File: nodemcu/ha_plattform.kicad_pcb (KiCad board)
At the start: 2 copper layers, 54 x 55 mm, 4 parts

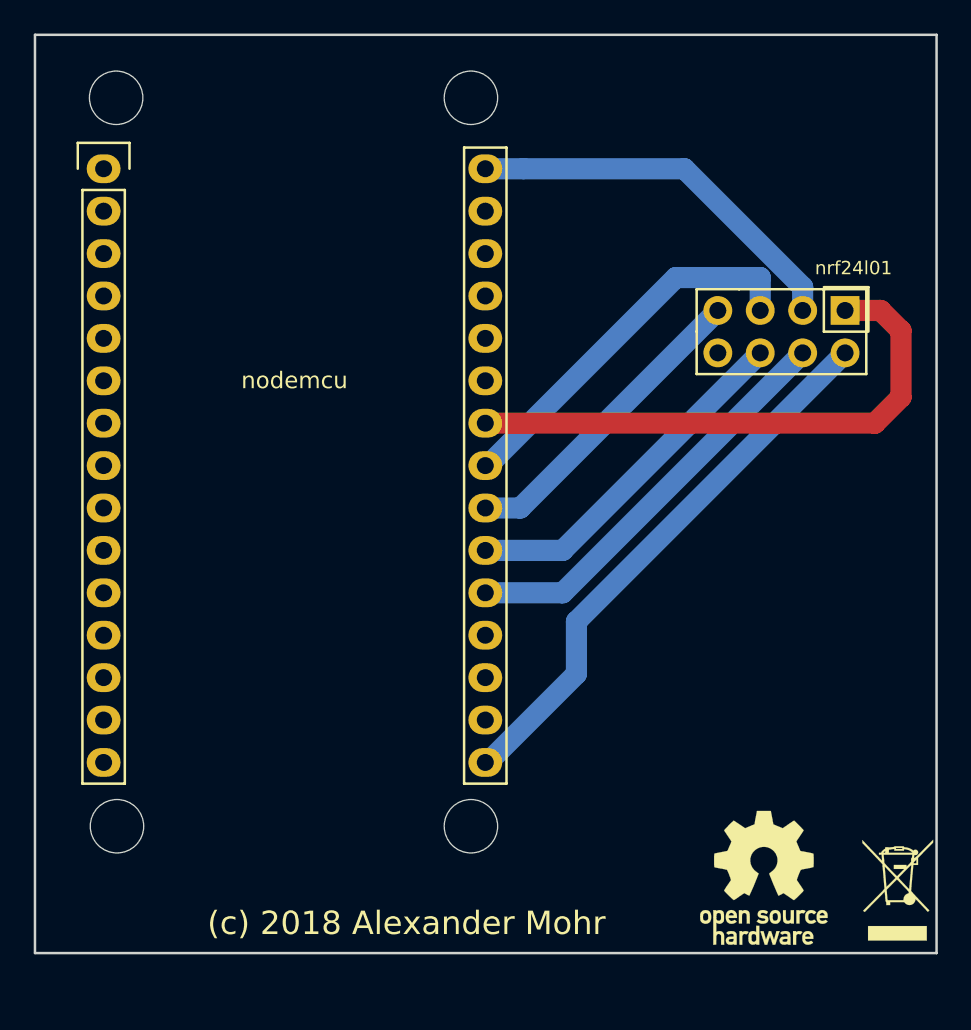
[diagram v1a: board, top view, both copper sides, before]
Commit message: fixed size for node mcu
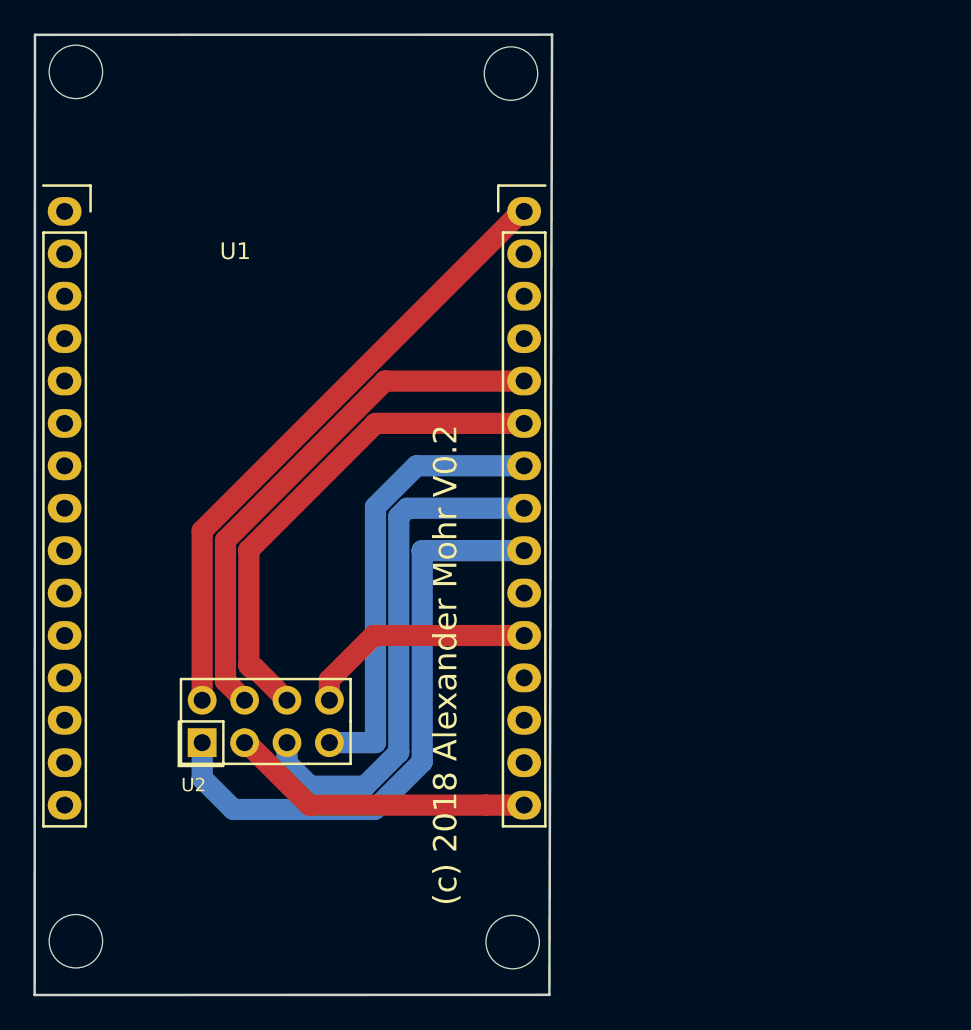
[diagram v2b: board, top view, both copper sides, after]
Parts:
- removed REF**: OSHW-Logo_7.5x8mm_SilkScreen, Symbol:OSHW-Logo_7.5x8mm_SilkScreen
- removed REF**: WEEE-Logo_4.2x6mm_SilkScreen, Symbol:WEEE-Logo_4.2x6mm_SilkScreen
- removed nodemcu: NodeMCU_Amica_R2, nodemcu:NodeMCU_Amica_R2
- removed nrf24l01: nRF24L01+, mysensors_radios:NRF24L01
- added U1: NodeMCU_Amica_R2, nodemcu:NodeMCU_personal, F.Cu at (20.6, 20.3)
- added U2: nRF24L01+, mysensors_radios:NRF24L01, F.Cu at (28.5, 63.9)
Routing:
- net (no net): track 0.00 -> 14.0 mm
- net Net-(U1-Pad21): track 21.4 -> 29.7 mm
- net Net-(U1-Pad23): track 23.1 -> 31.2 mm
- net Net-(U1-Pad22): track 18.8 -> 26.8 mm
- net Net-(U1-Pad20): track 25.0 -> 31.9 mm
- net Net-(U1-Pad30): track 23.3 -> 18.3 mm
- net Net-(U1-Pad16): track 33.5 -> 37.4 mm
- net Net-(U1-Pad24): track 33.4 -> 36.0 mm
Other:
- board size 54 x 55 mm -> 31 x 57.5 mm
- board text added: "(c) 2018 Alexander Mohr V0.2"
- board text removed: "(c) 2018 Alexander Mohr"
